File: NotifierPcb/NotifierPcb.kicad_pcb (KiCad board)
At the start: 2 copper layers, 81.6 x 97.9 mm, 32 parts, among them IC1 CD4067BEE4, IC2 ESP32-WROOM-32E__8MB_, J1 RC_433_MHZ_RF, J2 UART_Conn, J3 Power_Conn, J5 Vcc, J6 Vcc, U1 HT75xx-1-SOT89

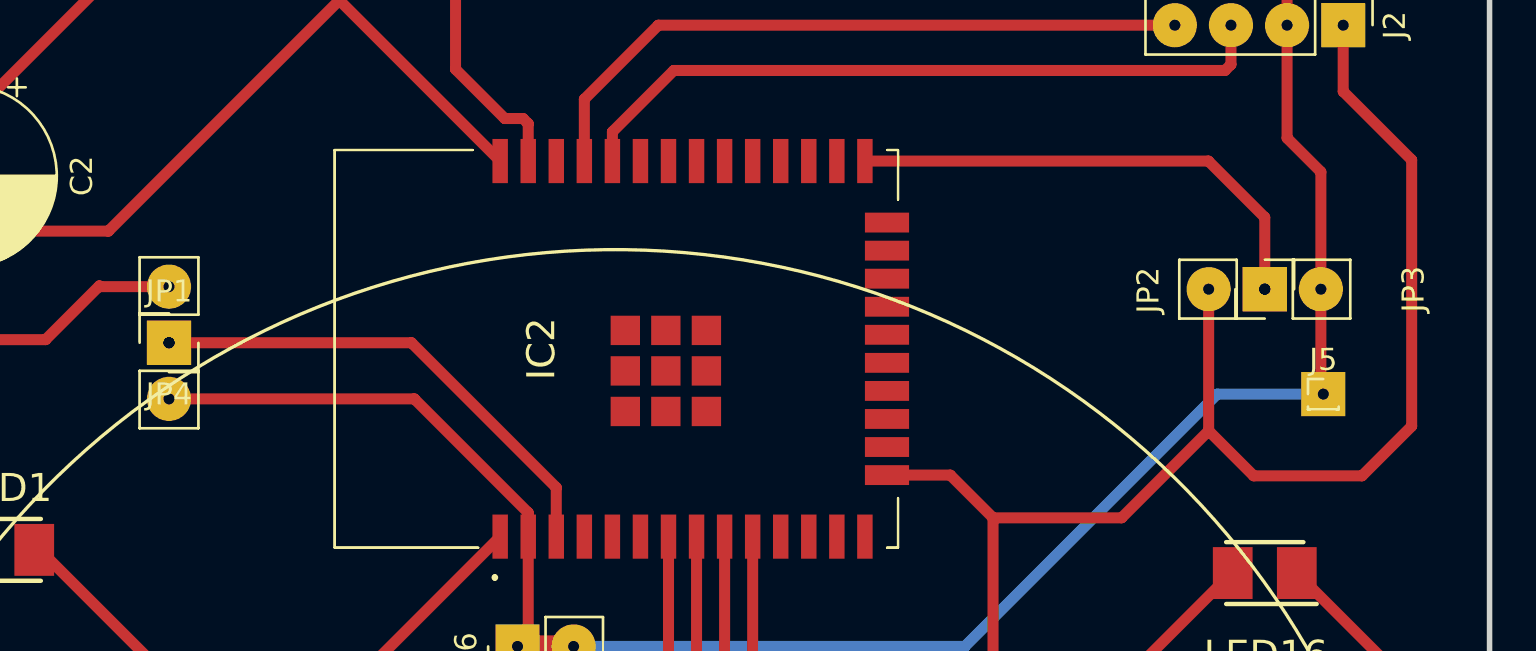
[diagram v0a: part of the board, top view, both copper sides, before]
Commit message: remove unused flag selectors (default pin state)
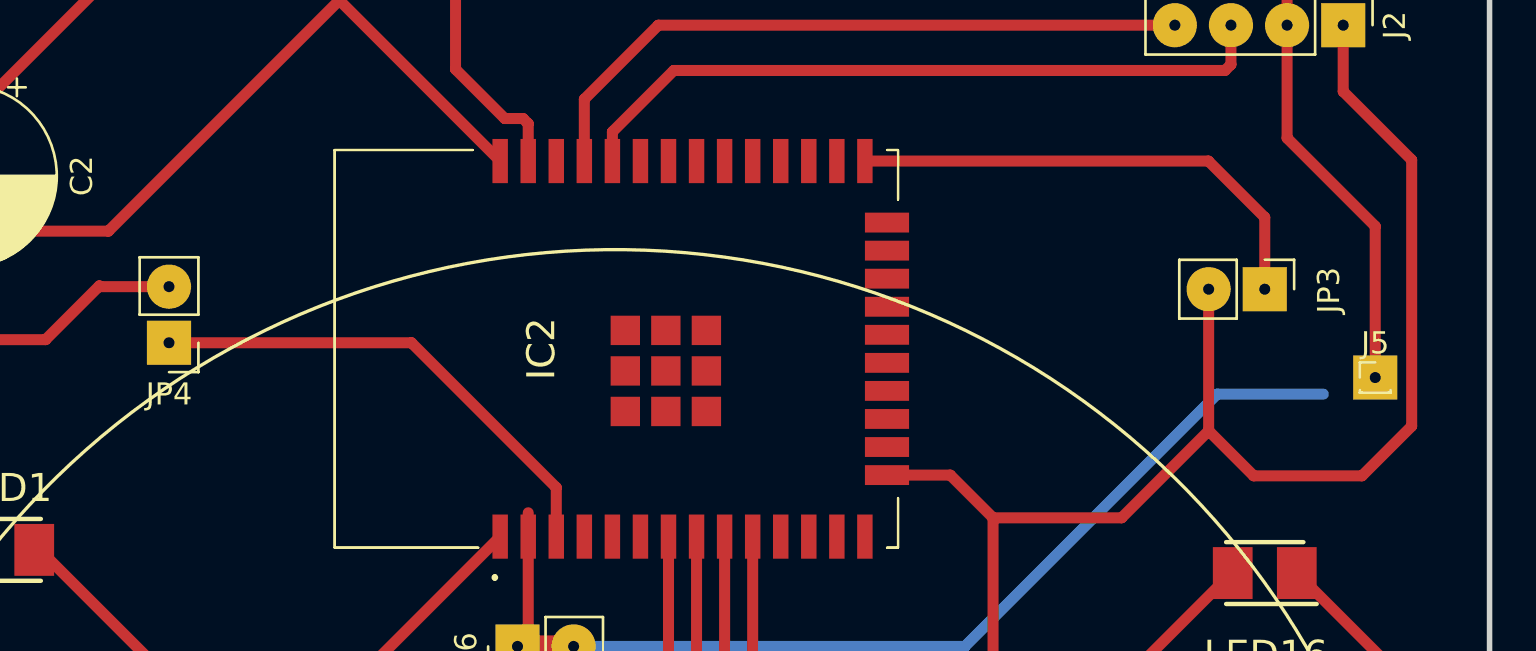
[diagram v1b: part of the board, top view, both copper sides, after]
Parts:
- removed JP1: Enable_Jumper, Connector_PinHeader_2.54mm:PinHeader_1x02_P2.54mm_Vertical
- removed JP2: Boot_Jumper_Flash, Connector_PinHeader_2.54mm:PinHeader_1x02_P2.54mm_Vertical
- moved J5 2.47 mm to (175.3, 65.3)
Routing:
- net +3.3V: track 258.5 -> 240.3 mm
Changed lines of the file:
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@@
-    )
-  )
-  (footprint "Connector_PinHeader_2.54mm:PinHeader_1x02_P2.54mm_Vertical" (layer "F.Cu")
-    (at 120.75 63.725)
-    (descr "Through hole straight pin header, 1x02, 2.54mm pitch, single row")
-    (tags "Through hole pin header THT 1x02 2.54mm single row")
-    (property "Sheetfile" "File: NotifierPcb.kicad_sch")
-    (property "Sheetname" "")
-    (attr through_hole)
-    (fp_text reference "JP1" (at 0 -2.33) (layer "F.SilkS")
-      (effects (font (size 1 1) (thickness 0.15)))
-    )
-    (fp_text value "Enable_Jumper" (at 0 4.87) (layer "F.Fab")
-      (effects (font (size 1 1) (thickness 0.15)))
-    )
-    (fp_text user "${REFERENCE}" (at 0 1.27 90) (layer "F.Fab")
-      (effects (font (size 1 1) (thickness 0.15)))
-    )
-    (fp_line (start -1.33 3.87) (end 1.33 3.87) (layer "F.SilkS") (width 0.12))
-    (fp_line (start -1.33 0) (end -1.33 -1.33) (layer "F.SilkS") (width 0.12))
-    (fp_line (start -1.33 -1.33) (end 0 -1.33) (layer "F.SilkS") (width 0.12))
-    (fp_line (start -1.33 1.27) (end 1.33 1.27) (layer "F.SilkS") (width 0.12))
-    (fp_line (start -1.33 1.27) (end -1.33 3.87) (layer "F.SilkS") (width 0.12))
-    (fp_line (start 1.33 1.27) (end 1.33 3.87) (layer "F.SilkS") (width 0.12))
-    (fp_line (start 1.8 -1.8) (end -1.8 -1.8) (layer "F.CrtYd") (width 0.05))
-    (fp_line (start 1.8 4.35) (end 1.8 -1.8) (layer "F.CrtYd") (width 0.05))
-    (fp_line (start -1.8 4.35) (end 1.8 4.35) (layer "F.CrtYd") (width 0.05))
-    (fp_line (start -1.8 -1.8) (end -1.8 4.35) (layer "F.CrtYd") (width 0.05))
-    (fp_line (start 1.27 -1.27) (end 1.27 3.81) (layer "F.Fab") (width 0.1))
-    (fp_line (start -1.27 3.81) (end -1.27 -0.635) (layer "F.Fab") (width 0.1))
-    (fp_line (start -1.27 -0.635) (end -0.635 -1.27) (layer "F.Fab") (width 0.1))
-    (fp_line (start -0.635 -1.27) (end 1.27 -1.27) (layer "F.Fab") (width 0.1))
-    (fp_line (start 1.27 3.81) (end -1.27 3.81) (layer "F.Fab") (width 0.1))
-    (pad "1" thru_hole rect (at 0 0) (size 2 2) (drill 0.5) (layers *.Cu *.Mask)
-      (net 23 "ESP32_EN") (pinfunction "A") (pintype "passive"))
-    (pad "2" thru_hole circle (at 0 2.54) (size 2 2) (drill 0.5) (layers *.Cu *.Mask)
-      (net 1 "+3.3V") (pinfunction "B") (pintype "passive"))
-    (model "${KICAD6_3DMODEL_DIR}/Connector_PinHeader_2.54mm.3dshapes/PinHeader_1x02_P2.54mm_Vertical.wrl"
-      (offset (xyz 0 0 0))
-      (scale (xyz 1 1 1))
-      (rotate (xyz 0 0 0))
     )
   )
@@
   )
   (footprint "Connector_PinHeader_1.00mm:PinHeader_1x01_P1.00mm_Vertical" (layer "F.Cu")
-    (at 173 66.05)
+    (at 175.35 65.3)
     (descr "Through hole straight pin header, 1x01, 1.00mm pitch, single row")
     (tags "Through hole pin header THT 1x01 1.00mm single row")
@@
     (property "Sheetname" "")
     (attr through_hole)
-    (fp_text reference "JP3" (at 0 -6.725 90) (layer "F.SilkS")
+    (fp_text reference "JP3" (at 0.05 -2.9 90) (layer "F.SilkS")
       (effects (font (size 1 1) (thickness 0.15)))
     )
@@
     )
   )
-  (footprint "Connector_PinHeader_2.54mm:PinHeader_1x02_P2.54mm_Vertical" (layer "F.Cu")
-    (at 170.35 61.3 90)
-    (descr "Through hole straight pin header, 1x02, 2.54mm pitch, single row")
-    (tags "Through hole pin header THT 1x02 2.54mm single row")
-    (property "Sheetfile" "File: NotifierPcb.kicad_sch")
-    (property "Sheetname" "")
-    (attr through_hole)
-    (fp_text reference "JP2" (at -0.05 -5.275 90) (layer "F.SilkS")
-      (effects (font (size 1 1) (thickness 0.15)))
-    )
-    (fp_text value "Boot_Jumper_Flash" (at -0.05 5.475 90) (layer "F.Fab")
-      (effects (font (size 1 1) (thickness 0.15)))
-    )
-    (fp_text user "${REFERENCE}" (at 0 1.27) (layer "F.Fab")
-      (effects (font (size 1 1) (thickness 0.15)))
-    )
-    (fp_line (start -1.33 1.27) (end -1.33 3.87) (layer "F.SilkS") (width 0.12))
-    (fp_line (start -1.33 0) (end -1.33 -1.33) (layer "F.SilkS") (width 0.12))
-    (fp_line (start -1.33 3.87) (end 1.33 3.87) (layer "F.SilkS") (width 0.12))
-    (fp_line (start -1.33 1.27) (end 1.33 1.27) (layer "F.SilkS") (width 0.12))
-    (fp_line (start -1.33 -1.33) (end 0 -1.33) (layer "F.SilkS") (width 0.12))
-    (fp_line (start 1.33 1.27) (end 1.33 3.87) (layer "F.SilkS") (width 0.12))
-    (fp_line (start 1.8 -1.8) (end -1.8 -1.8) (layer "F.CrtYd") (width 0.05))
-    (fp_line (start -1.8 -1.8) (end -1.8 4.35) (layer "F.CrtYd") (width 0.05))
-    (fp_line (start 1.8 4.35) (end 1.8 -1.8) (layer "F.CrtYd") (width 0.05))
-    (fp_line (start -1.8 4.35) (end 1.8 4.35) (layer "F.CrtYd") (width 0.05))
-    (fp_line (start 1.27 3.81) (end -1.27 3.81) (layer "F.Fab") (width 0.1))
-    (fp_line (start -1.27 -0.635) (end -0.635 -1.27) (layer "F.Fab") (width 0.1))
-    (fp_line (start -1.27 3.81) (end -1.27 -0.635) (layer "F.Fab") (width 0.1))
-    (fp_line (start -0.635 -1.27) (end 1.27 -1.27) (layer "F.Fab") (width 0.1))
-    (fp_line (start 1.27 -1.27) (end 1.27 3.81) (layer "F.Fab") (width 0.1))
-    (pad "1" thru_hole rect (at 0 0 90) (size 2 2) (drill 0.5) (layers *.Cu *.Mask)
-      (net 39 "BOOT") (pinfunction "A") (pintype "passive"))
-    (pad "2" thru_hole circle (at 0 2.54 90) (size 2 2) (drill 0.5) (layers *.Cu *.Mask)
-      (net 1 "+3.3V") (pinfunction "B") (pintype "passive"))
-    (model "${KICAD6_3DMODEL_DIR}/Connector_PinHeader_2.54mm.3dshapes/PinHeader_1x02_P2.54mm_Vertical.wrl"
-      (offset (xyz 0 0 0))
-      (scale (xyz 1 1 1))
-      (rotate (xyz 0 0 0))
-    )
-  )
   (footprint "SmdLed:LEDM3528X210N" (layer "F.Cu")
     (at 121.8 126.85)
@@
   (gr_rect (start 98.9 37.75) (end 180.525 135.65) (layer "Edge.Cuts") (width 0.25) (fill none))
   (segment (start 136.35 39.675) (end 136.15 39.475) (width 0.5) (layer "F.Cu") (net 1))
+  (segment (start 175.35 58.45) (end 175.35 65.3) (width 0.5) (layer "F.Cu") (net 1))
   (segment (start 137.01 76.985) (end 136.525 77.47) (width 1) (layer "F.Cu") (net 1))
   (segment (start 137.01 72.5) (end 137.01 76.985) (width 0.5) (layer "F.Cu") (net 1))
-  (segment (start 131.855 66.265) (end 120.75 66.265) (width 0.5) (layer "F.Cu") (net 1))
   (segment (start 171.36 46.06) (end 171.36 49.35) (width 0.5) (layer "F.Cu") (net 1))
   (segment (start 136.35 43.75) (end 169.05 43.75) (width 0.5) (layer "F.Cu") (net 1))
   (segment (start 137.01 72.5) (end 137.01 71.42) (width 0.5) (layer "F.Cu") (net 1))
   (segment (start 137 116.85) (end 135.325 118.525) (width 0.5) (layer "F.Cu") (net 1))
-  (segment (start 172.89 61.3) (end 172.89 65.94) (width 0.5) (layer "F.Cu") (net 1))
-  (segment (start 137.01 71.42) (end 131.855 66.265) (width 0.5) (layer "F.Cu") (net 1))
-  (segment (start 171.36 54.46) (end 172.89 55.99) (width 0.5) (layer "F.Cu") (net 1))
   (segment (start 125.747349 39.475) (end 111.55 53.672349) (width 0.5) (layer "F.Cu") (net 1))
   (segment (start 140 116.85) (end 137 116.85) (width 0.5) (layer "F.Cu") (net 1))
@@
   (segment (start 169.05 43.75) (end 171.36 46.06) (width 0.5) (layer "F.Cu") (net 1))
   (segment (start 171.36 49.35) (end 171.36 54.46) (width 0.5) (layer "F.Cu") (net 1))
-  (segment (start 172.89 65.94) (end 173 66.05) (width 0.5) (layer "F.Cu") (net 1))
   (segment (start 135.325 125.825) (end 137.75 128.25) (width 0.5) (layer "F.Cu") (net 1))
   (segment (start 135.325 118.525) (end 135.325 125.825) (width 0.5) (layer "F.Cu") (net 1))
   (segment (start 110.447349 54.775) (end 111.55 53.672349) (width 0.5) (layer "F.Cu") (net 1))
   (segment (start 147.55 124.95) (end 147.55 110.97) (width 0.5) (layer "F.Cu") (net 1))
-  (segment (start 172.89 55.99) (end 172.89 61.3) (width 0.5) (layer "F.Cu") (net 1))
   (segment (start 132.45 115.65) (end 135.325 118.525) (width 0.5) (layer "F.Cu") (net 1))
+  (segment (start 171.36 54.46) (end 175.35 58.45) (width 0.5) (layer "F.Cu") (net 1))
   (segment (start 132.45 110.97) (end 132.45 115.65) (width 0.5) (layer "F.Cu") (net 1))
   (segment (start 144.25 128.25) (end 147.55 124.95) (width 0.5) (layer "F.Cu") (net 1))
@@
     (connect_pads (clearance 0))
     (min_thickness 0.254)
-    (keepout (tracks not_allowed) (vias not_allowed) (pads not_allowed ) (copperpour not_allowed) (footprints not_allowed))
+    (keepout (tracks not_allowed) (vias not_allowed) (pads not_allowed) (copperpour not_allowed) (footprints not_allowed))
     (fill (thermal_gap 0.508) (thermal_bridge_width 0.508))
     (polygon
@@
     (members
       8ef20554-2ff2-448f-88c7-9550c8c3dd59
-      da12aa73-c104-4a36-8c94-daed5ec0e9e7
-    )
-  )
+    )
+  )
